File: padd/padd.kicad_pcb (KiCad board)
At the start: 2 copper layers, 128.6 x 120.6 mm, 71 parts, among them SW1 RotaryEncoder_Switch, SW2 RotaryEncoder_Switch, U1 Elite-C

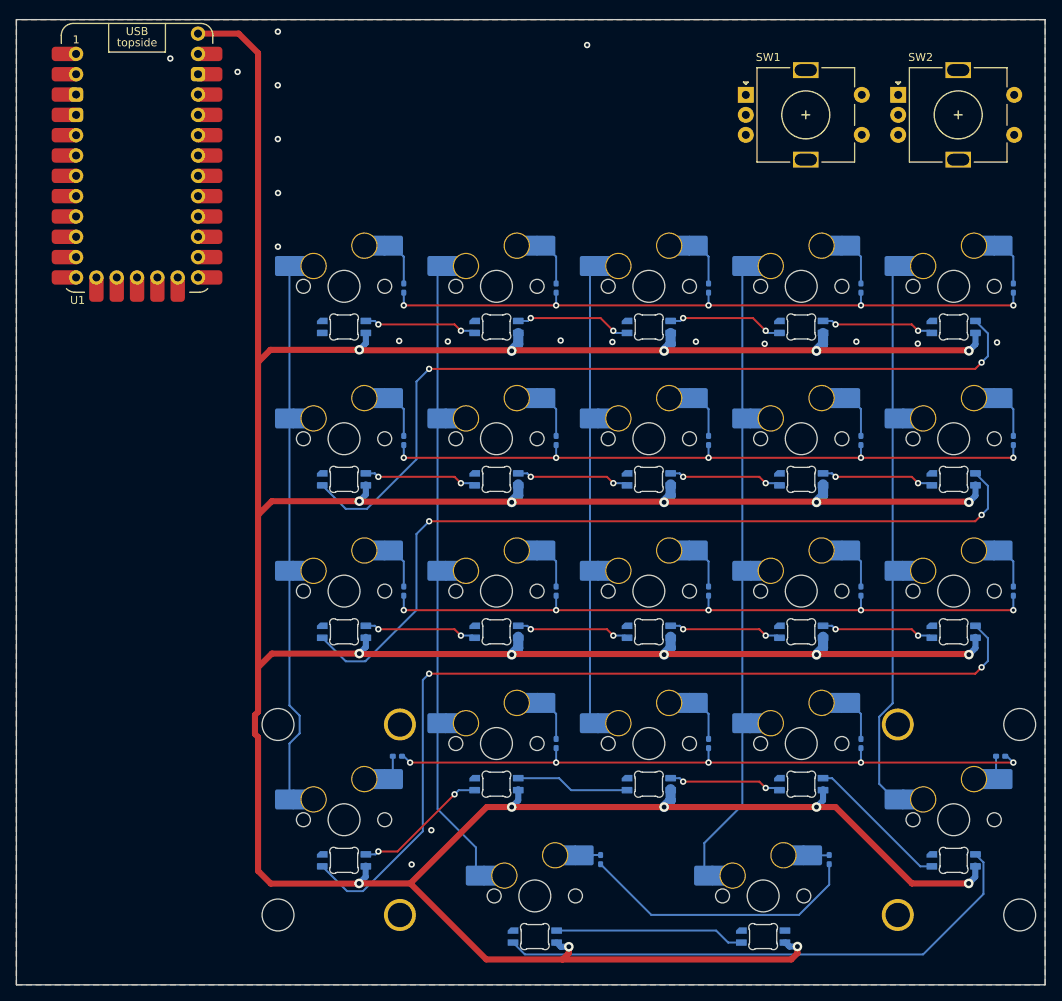
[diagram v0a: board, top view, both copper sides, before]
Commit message: move to rp2040 onboard
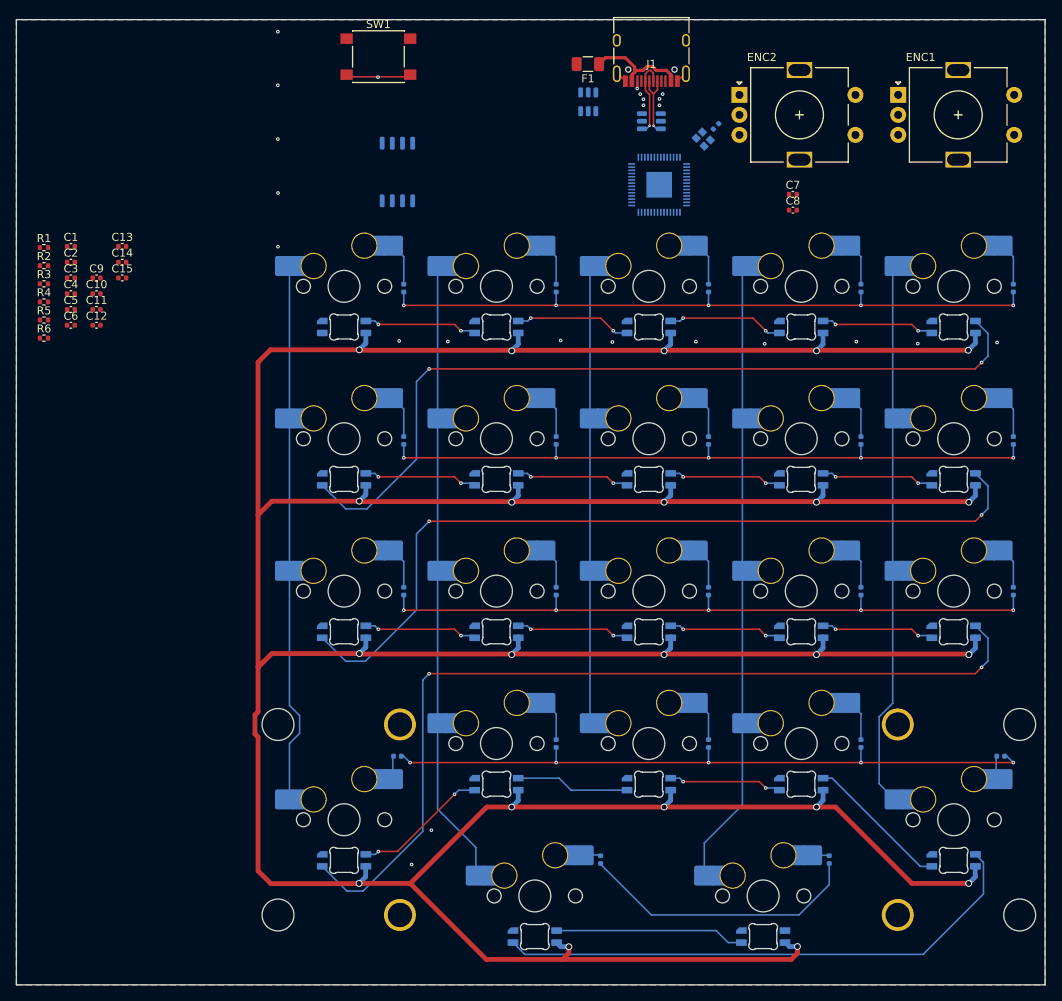
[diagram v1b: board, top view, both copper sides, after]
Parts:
- removed SW2: RotaryEncoder_Switch, Rotary_Encoder:RotaryEncoder_Alps_EC11E-Switch_Vertical_H20mm
- added C1: 10u, Capacitor_SMD:C_0402_1005Metric, F.Cu at (29.8, 92.6)
- added C10: 100n, Capacitor_SMD:C_0402_1005Metric, F.Cu at (33.0, 98.6)
- added C11: 100n, Capacitor_SMD:C_0402_1005Metric, F.Cu at (33.0, 100.5)
- added C12: 100n, Capacitor_SMD:C_0402_1005Metric, F.Cu at (33.0, 102.5)
- added C13: 100n, Capacitor_SMD:C_0402_1005Metric, F.Cu at (36.3, 92.6)
- added C14: 1u, Capacitor_SMD:C_0402_1005Metric, F.Cu at (36.3, 94.6)
- added C15: 22p, Capacitor_SMD:C_0402_1005Metric, F.Cu at (36.3, 96.6)
- added C16: 22p, Capacitor_SMD:C_0402_1005Metric, B.Cu at (110.5, 77.6)
- added C2: 10u, Capacitor_SMD:C_0402_1005Metric, F.Cu at (29.8, 94.6)
- added C3: 100n, Capacitor_SMD:C_0402_1005Metric, F.Cu at (29.8, 96.6)
- added C4: 100n, Capacitor_SMD:C_0402_1005Metric, F.Cu at (29.8, 98.6)
- added C5: 100n, Capacitor_SMD:C_0402_1005Metric, F.Cu at (29.8, 100.5)
- added C6: 1u, Capacitor_SMD:C_0402_1005Metric, F.Cu at (29.8, 102.5)
- added C7: 100n, Capacitor_SMD:C_0402_1005Metric, F.Cu at (120.1, 86.1)
- added C8: 100n, Capacitor_SMD:C_0402_1005Metric, F.Cu at (120.1, 88.1)
- added C9: 100n, Capacitor_SMD:C_0402_1005Metric, F.Cu at (33.0, 96.6)
- added ENC1: RotaryEncoder_Switch, Rotary_Encoder:RotaryEncoder_Alps_EC11E-Switch_Vertical_H20mm, F.Cu at (133.2, 73.7)
- added ENC2: RotaryEncoder_Switch, Rotary_Encoder:RotaryEncoder_Alps_EC11E-Switch_Vertical_H20mm, F.Cu at (113.4, 73.7)
- added F1: 500mA, Fuse:Fuse_1206_3216Metric, F.Cu at (94.5, 69.8)
- added J1: USB_C_Receptacle_USB2.0, Connector_USB:USB_C_Receptacle_HRO_TYPE-C-31-M-12, F.Cu at (102.4, 67.9)
- added R1: 1k, Resistor_SMD:R_0402_1005Metric, F.Cu at (26.5, 92.8)
- added R2: 5.1k, Resistor_SMD:R_0402_1005Metric, F.Cu at (26.5, 95.1)
- added R3: 5.1k, Resistor_SMD:R_0402_1005Metric, F.Cu at (26.5, 97.3)
- added R4: DNF, Resistor_SMD:R_0402_1005Metric, F.Cu at (26.5, 99.6)
- added R5: 1k, Resistor_SMD:R_0402_1005Metric, F.Cu at (26.5, 101.8)
- added R6: 220, Resistor_SMD:R_0402_1005Metric, F.Cu at (26.5, 104.1)
- added U2: W25Q128JVS, Package_SO:SOIC-8_5.23x5.23mm_P1.27mm, B.Cu at (70.6, 83.3)
- added U3: SRV05-4, PCM_marbastlib-various:SOT-23-6-routable, B.Cu at (102.4, 77.0)
- added U4: XC6206PxxxMR, PCM_marbastlib-various:SOT-23-6-routable, B.Cu at (94.5, 74.6)
- added Y1: Crystal_GND24_Small, Crystal:Crystal_SMD_2016-4Pin_2.0x1.6mm, B.Cu at (108.9, 79.2)
- D1, D10, D11, D12, D13, D14, D15, D16, D17, D18, D19, D2, D20, D21, D22, D3, D4, D5, D6, D7, D8, D9: footprint Diode_SMD:D_0402_1005Metric_Pad0.77x0.64mm_HandSolder -> Diode_SMD:D_0402_1005Metric
- SW1: value RotaryEncoder_Switch -> SW_Push; footprint Rotary_Encoder:RotaryEncoder_Alps_EC11E-Switch_Vertical_H20mm -> Button_Switch_SMD:SW_Push_1P1T_NO_6x6mm_H9.5mm
- U1: value Elite-C -> RP2040; footprint PCM_marbastlib-xp-promicroish:Elite-C_ACH -> Package_DFN_QFN:QFN-56-1EP_7x7mm_P0.4mm_EP3.2x3.2mm; moved to B.Cu
- moved U1 65.3 mm to (103.4, 84.9), turned to -90 degrees
- moved SW1 46.2 mm to (68.3, 68.9)
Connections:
- net /COL0 renamed COL0
- net /COL2 renamed COL1
- net /COL3 renamed COL2
- net /COL4 renamed COL3
- net /COL5 renamed COL4
- net /ROW0 renamed ROW0
- net /ROW1 renamed ROW1
- net /ROW2 renamed ROW2
- net /ROW3 renamed ROW3
- net /ROW4 renamed ROW4
- net Net-(LED10-DOUT) renamed LED_R1_DOUT
- net Net-(LED15-DOUT) renamed LED_R2_DOUT
- net Net-(LED20-DOUT) renamed LED_R3_DOUT
- net Net-(LED5-DOUT) renamed LED_R0_DOUT
- LED1 pad 3: /LED_DIN -> Net-(LED1-DIN)
- U1 pad 1: unconnected-(U1-D3-TX-Pad1) -> +3V3
- U1 pad 10: unconnected-(U1-E6-Pad10) -> +3V3
- U1 pad 14: GND -> unconnected-(U1-GPIO11-Pad14)
- U1 pad 19: unconnected-(U1-F6-Pad19) -> GND
- U1 pad 20: unconnected-(U1-F7-Pad20) -> XIN
- U1 pad 21: unconnected-(U1-B1-Pad21) -> XOUT
- U1 pad 22: unconnected-(U1-B3-Pad22) -> +3V3
- U1 pad 23: unconnected-(U1-B2-Pad23) -> +1V1
- U1 pad 24: unconnected-(U1-B6-Pad24) -> SWCLK
- U1 pad 25: unconnected-(U1-B7-Pad25) -> SWD
- U1 pad 26: unconnected-(U1-D5-Pad26) -> ~{RESET}
- U1 pad 3: GND -> unconnected-(U1-GPIO1-Pad3)
- U1 pad 30: +5V -> unconnected-(U1-GPIO19-Pad30)
- U1 pad 4: GND -> unconnected-(U1-GPIO2-Pad4)
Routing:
- net +5V: track 587.3 -> 540.0 mm
- net VBUS: track 0.00 -> 13.2 mm
- net D-: track 0.00 -> 10.1 mm, vias 0 -> 1
- net GND: track 1.30 -> 10.8 mm, vias 19 -> 23
- net D+: track 0.00 -> 8.66 mm, vias 0 -> 1
- net Net-(J1-CC2): track 0.00 -> 0.93 mm, vias 0 -> 1
